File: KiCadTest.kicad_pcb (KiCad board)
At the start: 2 copper layers, 25.4 x 68.6 mm, 6 parts, among them J1 Conn_02x25_Odd_Even, U1 25LCxxx, U2 74HC4051, U3 25LCxxx

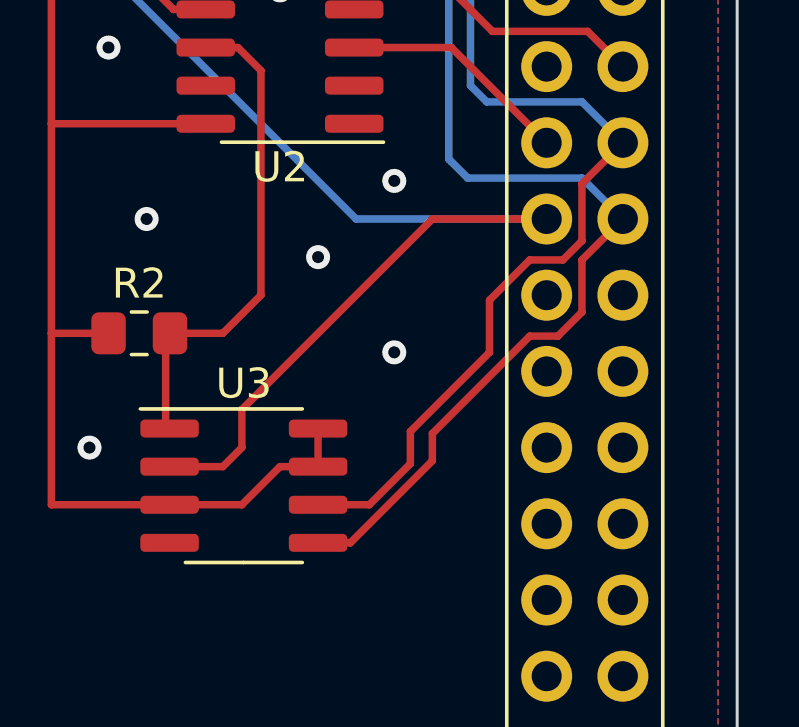
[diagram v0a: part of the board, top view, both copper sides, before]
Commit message: Reroute some PCB tracks and switch 5V for VDD
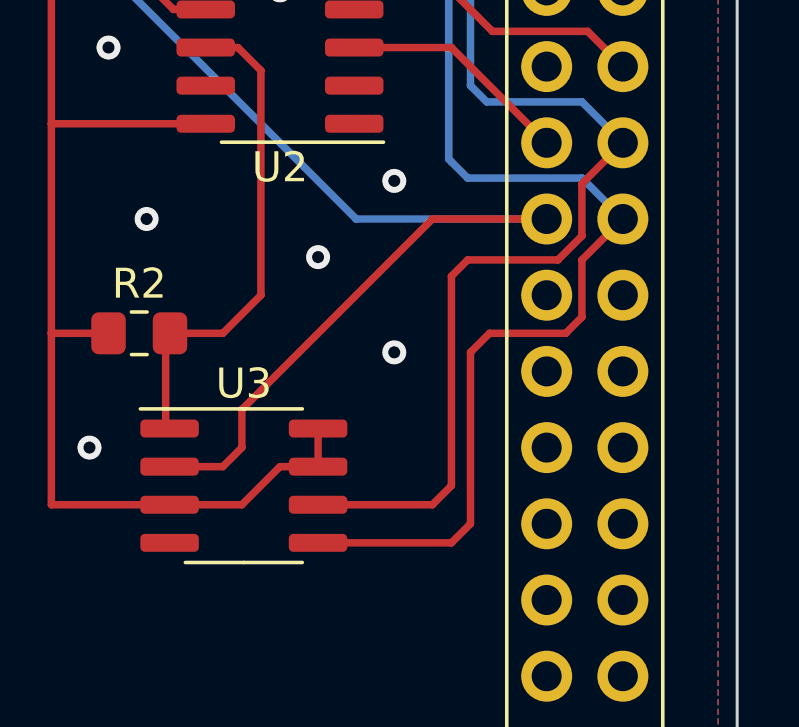
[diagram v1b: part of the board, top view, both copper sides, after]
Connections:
- net +5V renamed VDD
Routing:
- net SPI4_MOSI: track 43.1 -> 46.0 mm
- net SPI4_SCK: track 43.8 -> 46.1 mm
